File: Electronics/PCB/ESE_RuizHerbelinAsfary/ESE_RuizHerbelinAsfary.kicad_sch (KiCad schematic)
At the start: 0 parts

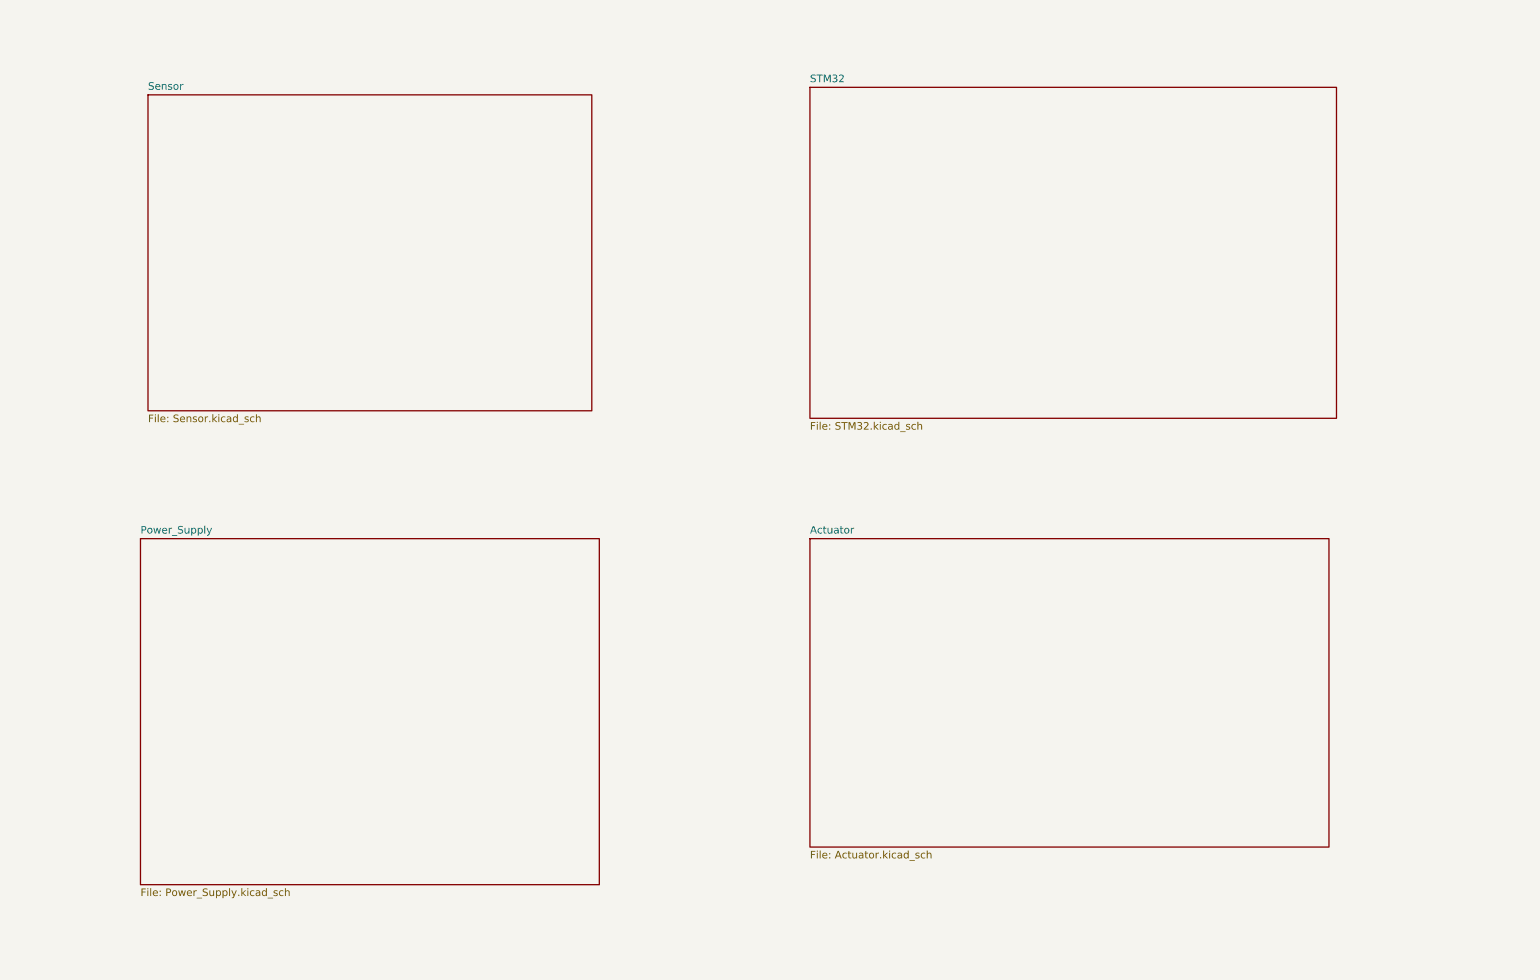
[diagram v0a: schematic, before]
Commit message: added test pin
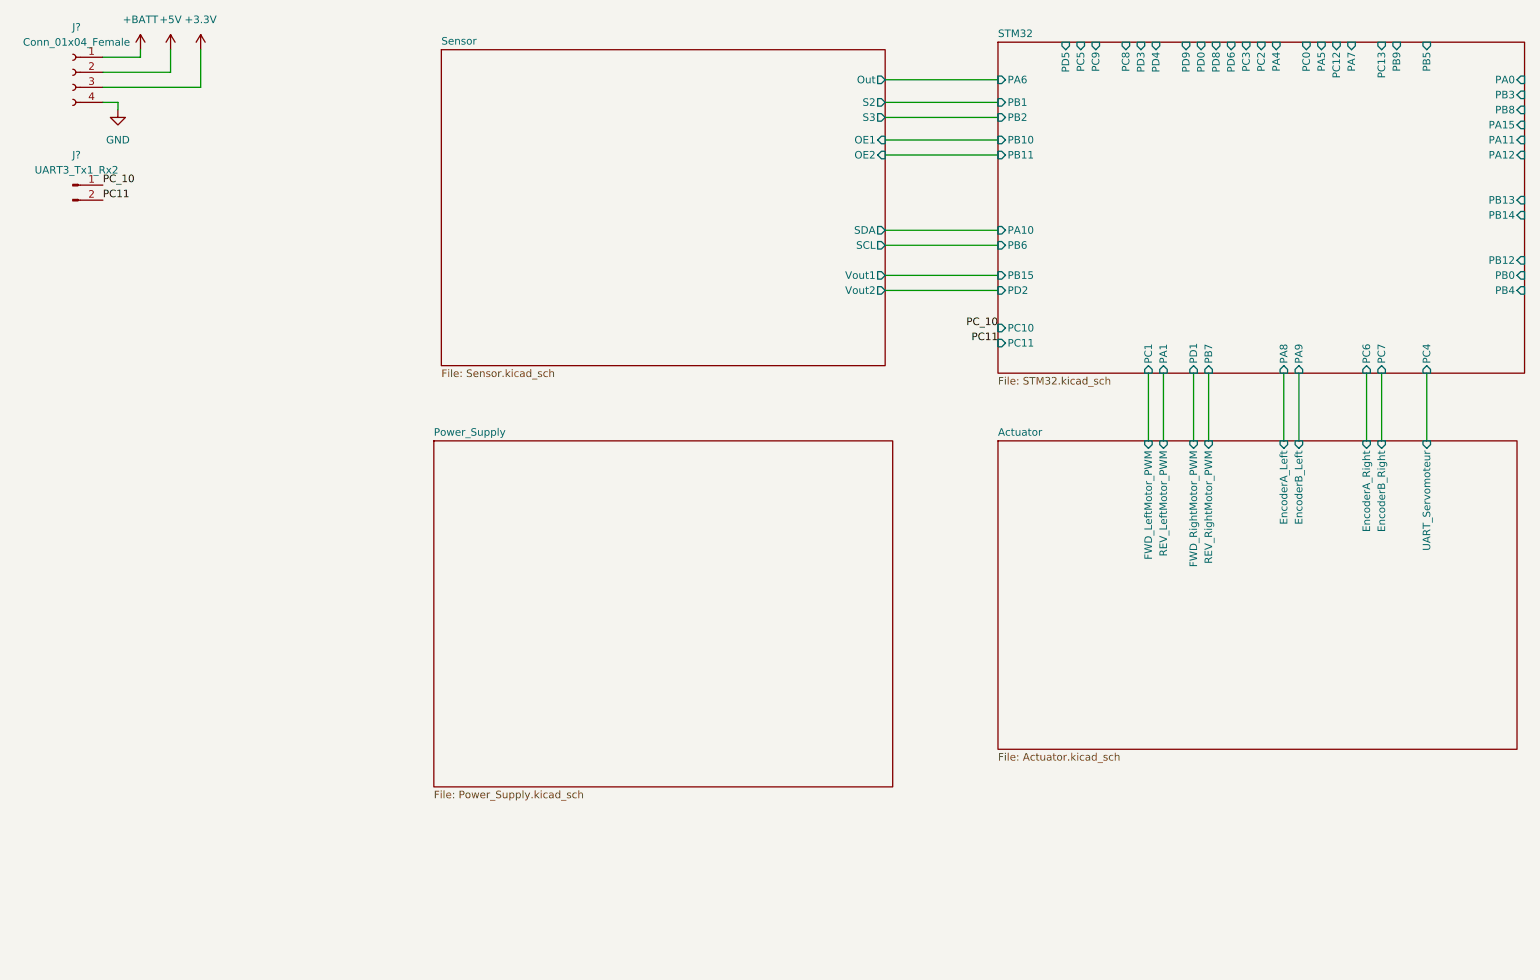
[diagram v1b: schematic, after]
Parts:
- added J?: Conn_01x04_Female, symbol Connector:Conn_01x04_Female
- added J?: UART3_Tx1_Rx2, symbol Connector:Conn_01x02_Male
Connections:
- new net +3.3V: J?.3 (Pin_3)
- new net +5V: J?.2 (Pin_2)
- new net +BATT: J?.1 (Pin_1)
- new net GND: J?.4 (Pin_4)
- new net PC11: J?.2 (Pin_2)
- new net PC_10: J?.1 (Pin_1)
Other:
- sheet Actuator ports: added EncoderA_Left, EncoderA_Right, EncoderB_Left, EncoderB_Right, FWD_LeftMotor_PWM, FWD_RightMotor_PWM, REV_LeftMotor_PWM, REV_RightMotor_PWM, UART_Servomoteur; removed none
- sheet STM32 ports: added PA0, PA1, PA10, PA11, PA12, PA15, PA4, PA5, PA6, PA7, PA8, PA9, PB0, PB1, PB10, PB11, PB12, PB13, PB14, PB15, PB2, PB3, PB4, PB5, PB6, PB7, PB8, PB9, PC0, PC1, PC10, PC11, PC12, PC13, PC2, PC3, PC4, PC5, PC6, PC7, PC8, PC9, PD0, PD1, PD2, PD3, PD4, PD5, PD6, PD8, PD9; removed none
- sheet Sensor ports: added OE1, OE2, Out, S2, S3, SCL, SDA, Vout1, Vout2; removed none

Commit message: PCB finished
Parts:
- added J101, J104: I2C1, symbol Connector:Conn_01x04_Male
- added J105: MTRX_test, symbol Connector:Conn_01x04_Female
- J102: renamed from J?; value Conn_01x04_Female -> MTRX_test
- J103: renamed from J?; value UART3_Tx1_Rx2 -> UART3
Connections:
- net +3.3V: now also J105.3 (Pin_3)
- net +5V: now also J101.2 (Pin_2), J104.2 (Pin_2), J105.2 (Pin_2)
- net +BATT: now also J105.1 (Pin_1)
- net GND: now also J101.1 (Pin_1), J104.1 (Pin_1), J105.4 (Pin_4)
- net PC11 renamed UART_Rx
- net PC_10 renamed UART_Tx
- new net SCL: J101.4 (Pin_4), J104.4 (Pin_4)
- new net SDA: J101.3 (Pin_3), J104.3 (Pin_3)
- no-connect marks 0 -> 31
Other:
- sheet STM32 ports: added PC14, PC15; removed PA0, PC3
- moved on the sheet: J102, J103

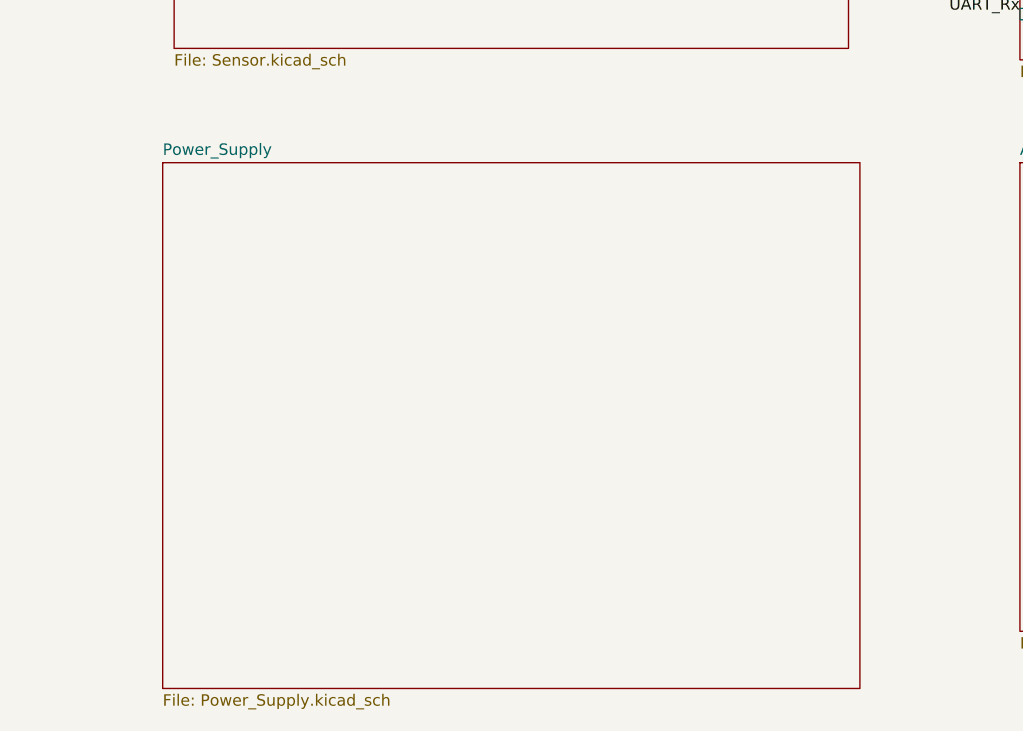
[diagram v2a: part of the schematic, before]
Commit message: added solderbridge before and after the driver
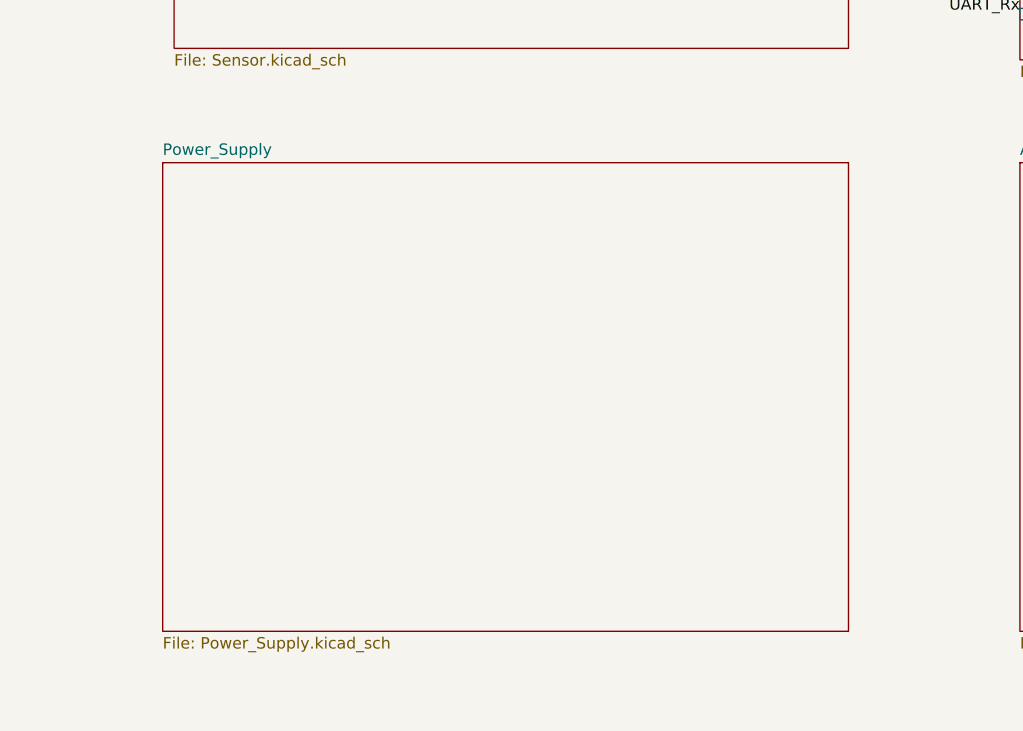
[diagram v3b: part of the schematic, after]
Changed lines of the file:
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@@
     )
   )
-  (sheet (at 82.55 91.44) (size 77.47 58.42) (fields_autoplaced)
+  (sheet (at 82.55 91.44) (size 76.2 52.07) (fields_autoplaced)
     (stroke (width 0.1524) (type solid) (color 0 0 0 0))
     (fill (color 0 0 0 0.0000))
@@
       (effects (font (size 1.27 1.27)) (justify left bottom))
     )
-    (property "Sheet file" "Power_Supply.kicad_sch" (id 1) (at 82.55 150.4446 0)
+    (property "Sheet file" "Power_Supply.kicad_sch" (id 1) (at 82.55 144.0946 0)
       (effects (font (size 1.27 1.27)) (justify left top))
     )
@@
       (reference "JP304") (unit 1) (value "SolderJumper_2_Open") (footprint "Jumper:SolderJumper-2_P1.3mm_Open_TrianglePad1.0x1.5mm")
     )
+    (path "/40bbd4bc-312d-49bd-88f6-2ab9dae3d019/5dc02104-21f7-4f53-9061-38b6726af5c5"
+      (reference "JP501") (unit 1) (value "SolderJumper_2_Open") (footprint "")
+    )
+    (path "/40bbd4bc-312d-49bd-88f6-2ab9dae3d019/54a8f4e5-28a8-4fc1-90d3-f20d46e96ad6"
+      (reference "JP502") (unit 1) (value "SolderJumper_2_Open") (footprint "")
+    )
+    (path "/40bbd4bc-312d-49bd-88f6-2ab9dae3d019/bc740fd3-668f-4267-ac36-312e4e5fa39b"
+      (reference "JP503") (unit 1) (value "SolderJumper_2_Open") (footprint "")
+    )
+    (path "/40bbd4bc-312d-49bd-88f6-2ab9dae3d019/83365208-79ca-41b0-93fa-216402934a32"
+      (reference "JP504") (unit 1) (value "SolderJumper_2_Open") (footprint "")
+    )
+    (path "/40bbd4bc-312d-49bd-88f6-2ab9dae3d019/8659013f-857b-45d1-95b7-d7905afd2a1a"
+      (reference "JP505") (unit 1) (value "SolderJumper_2_Open") (footprint "")
+    )
+    (path "/40bbd4bc-312d-49bd-88f6-2ab9dae3d019/a0cccba3-27a4-4ade-bfe9-13adaf4125e9"
+      (reference "JP506") (unit 1) (value "SolderJumper_2_Open") (footprint "")
+    )
+    (path "/40bbd4bc-312d-49bd-88f6-2ab9dae3d019/a5f7af30-ad0f-4f3a-ab85-fb2520afcaa8"
+      (reference "JP507") (unit 1) (value "SolderJumper_2_Open") (footprint "")
+    )
+    (path "/40bbd4bc-312d-49bd-88f6-2ab9dae3d019/6d9ec327-a8f1-4d49-b44f-b2ca5f46cbe0"
+      (reference "JP508") (unit 1) (value "SolderJumper_2_Open") (footprint "")
+    )
     (path "/6b2f643a-955a-47ef-920e-70e4f09a6662/29b03a20-4b8e-4936-9a55-9ac0bf668a19"

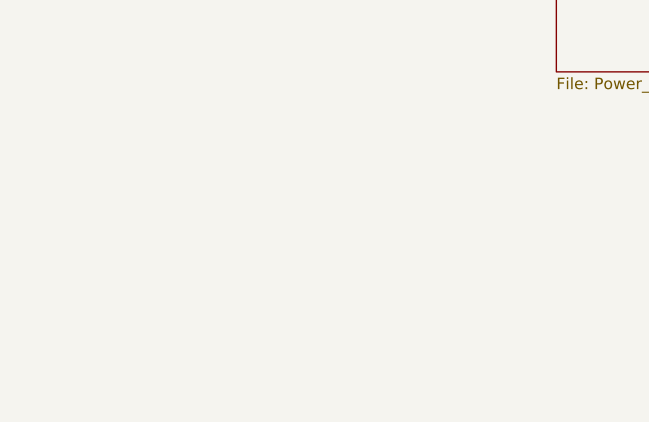
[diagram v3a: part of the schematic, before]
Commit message: added mounting hole
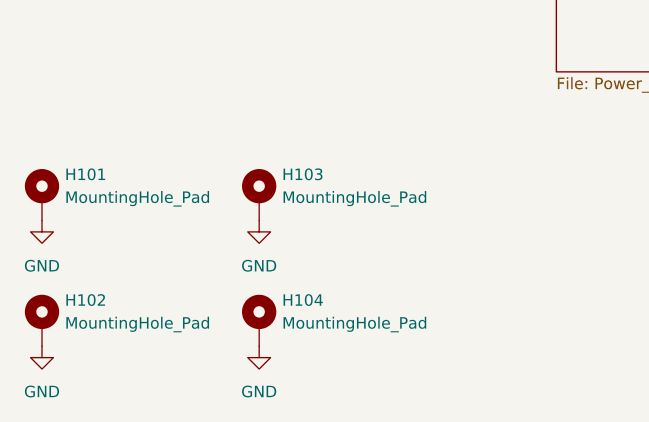
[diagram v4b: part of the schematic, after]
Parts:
- added H101, H102, H103, H104: MountingHole_Pad, symbol Mechanical:MountingHole_Pad
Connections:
- net GND: now also H101.1, H102.1, H103.1, H104.1
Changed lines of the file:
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@@
     (effects (font (size 1.27 1.27)) (justify left bottom))
+  )
+  (symbol (lib_id "power:GND") (at 49.53 160.02 0) (unit 1)
+    (in_bom yes) (on_board yes) (fields_autoplaced)
+    (property "Reference" "#PWR0115" (id 0) (at 49.53 166.37 0)
+      (effects (font (size 1.27 1.27)) hide)
+    )
+    (property "Value" "GND" (id 1) (at 49.53 165.1 0))
+    (property "Footprint" "" (id 2) (at 49.53 160.02 0)
+      (effects (font (size 1.27 1.27)) hide)
+    )
+    (property "Datasheet" "" (id 3) (at 49.53 160.02 0)
+      (effects (font (size 1.27 1.27)) hide)
+    )
+    (pin "1")
   )
   (symbol (lib_id "power:GND") (at 39.37 106.68 0) (unit 1)
@@
     )
     (property "Datasheet" "" (id 3) (at 39.37 106.68 0)
+      (effects (font (size 1.27 1.27)) hide)
+    )
+    (pin "1")
+  )
+  (symbol (lib_id "power:GND") (at 49.53 173.99 0) (unit 1)
+    (in_bom yes) (on_board yes) (fields_autoplaced)
+    (property "Reference" "#PWR0116" (id 0) (at 49.53 180.34 0)
+      (effects (font (size 1.27 1.27)) hide)
+    )
+    (property "Value" "GND" (id 1) (at 49.53 179.07 0))
+    (property "Footprint" "" (id 2) (at 49.53 173.99 0)
+      (effects (font (size 1.27 1.27)) hide)
+    )
+    (property "Datasheet" "" (id 3) (at 49.53 173.99 0)
       (effects (font (size 1.27 1.27)) hide)
     )
@@
     (pin "1")
   )
+  (symbol (lib_id "Mechanical:MountingHole_Pad") (at 49.53 157.48 0) (unit 1)
+    (in_bom yes) (on_board yes) (fields_autoplaced)
+    (property "Reference" "H103" (id 0) (at 52.07 154.9399 0)
+      (effects (font (size 1.27 1.27)) (justify left))
+    )
+    (property "Value" "MountingHole_Pad" (id 1) (at 52.07 157.4799 0)
+      (effects (font (size 1.27 1.27)) (justify left))
+    )
+    (property "Footprint" "" (id 2) (at 49.53 157.48 0)
+      (effects (font (size 1.27 1.27)) hide)
+    )
+    (property "Datasheet" "~" (id 3) (at 49.53 157.48 0)
+      (effects (font (size 1.27 1.27)) hide)
+    )
+    (pin "1")
+  )
   (symbol (lib_id "power:GND") (at 35.56 59.69 0) (unit 1)
     (in_bom yes) (on_board yes) (fields_autoplaced)
@@
     (pin "2")
   )
+  (symbol (lib_id "Mechanical:MountingHole_Pad") (at 25.4 171.45 0) (unit 1)
+    (in_bom yes) (on_board yes) (fields_autoplaced)
+    (property "Reference" "H102" (id 0) (at 27.94 168.9099 0)
+      (effects (font (size 1.27 1.27)) (justify left))
+    )
+    (property "Value" "MountingHole_Pad" (id 1) (at 27.94 171.4499 0)
+      (effects (font (size 1.27 1.27)) (justify left))
+    )
+    (property "Footprint" "" (id 2) (at 25.4 171.45 0)
+      (effects (font (size 1.27 1.27)) hide)
+    )
+    (property "Datasheet" "~" (id 3) (at 25.4 171.45 0)
+      (effects (font (size 1.27 1.27)) hide)
+    )
+    (pin "1")
+  )
   (symbol (lib_id "power:+5V") (at 44.45 25.4 0) (unit 1)
     (in_bom yes) (on_board yes) (fields_autoplaced)
@@
     (pin "1")
   )
+  (symbol (lib_id "power:GND") (at 25.4 173.99 0) (unit 1)
+    (in_bom yes) (on_board yes) (fields_autoplaced)
+    (property "Reference" "#PWR0114" (id 0) (at 25.4 180.34 0)
+      (effects (font (size 1.27 1.27)) hide)
+    )
+    (property "Value" "GND" (id 1) (at 25.4 179.07 0))
+    (property "Footprint" "" (id 2) (at 25.4 173.99 0)
+      (effects (font (size 1.27 1.27)) hide)
+    )
+    (property "Datasheet" "" (id 3) (at 25.4 173.99 0)
+      (effects (font (size 1.27 1.27)) hide)
+    )
+    (pin "1")
+  )
   (symbol (lib_id "power:+5V") (at 35.56 85.09 0) (unit 1)
     (in_bom yes) (on_board yes) (fields_autoplaced)
@@
     )
     (property "Datasheet" "" (id 3) (at 35.56 85.09 0)
+      (effects (font (size 1.27 1.27)) hide)
+    )
+    (pin "1")
+  )
+  (symbol (lib_id "Mechanical:MountingHole_Pad") (at 25.4 157.48 0) (unit 1)
+    (in_bom yes) (on_board yes) (fields_autoplaced)
+    (property "Reference" "H101" (id 0) (at 27.94 154.9399 0)
+      (effects (font (size 1.27 1.27)) (justify left))
+    )
+    (property "Value" "MountingHole_Pad" (id 1) (at 27.94 157.4799 0)
+      (effects (font (size 1.27 1.27)) (justify left))
+    )
+    (property "Footprint" "" (id 2) (at 25.4 157.48 0)
+      (effects (font (size 1.27 1.27)) hide)
+    )
+    (property "Datasheet" "~" (id 3) (at 25.4 157.48 0)
       (effects (font (size 1.27 1.27)) hide)
     )
@@
     (pin "4")
   )
+  (symbol (lib_id "Mechanical:MountingHole_Pad") (at 49.53 171.45 0) (unit 1)
+    (in_bom yes) (on_board yes) (fields_autoplaced)
+    (property "Reference" "H104" (id 0) (at 52.07 168.9099 0)
+      (effects (font (size 1.27 1.27)) (justify left))
+    )
+    (property "Value" "MountingHole_Pad" (id 1) (at 52.07 171.4499 0)
+      (effects (font (size 1.27 1.27)) (justify left))
+    )
+    (property "Footprint" "" (id 2) (at 49.53 171.45 0)
+      (effects (font (size 1.27 1.27)) hide)
+    )
+    (property "Datasheet" "~" (id 3) (at 49.53 171.45 0)
+      (effects (font (size 1.27 1.27)) hide)
+    )
+    (pin "1")
+  )
   (symbol (lib_id "Connector:Conn_01x04_Male") (at 27.94 88.9 0) (unit 1)
     (in_bom yes) (on_board yes) (fields_autoplaced)
@@
     )
     (property "Datasheet" "" (id 3) (at 49.53 25.4 0)
+      (effects (font (size 1.27 1.27)) hide)
+    )
+    (pin "1")
+  )
+  (symbol (lib_id "power:GND") (at 25.4 160.02 0) (unit 1)
+    (in_bom yes) (on_board yes) (fields_autoplaced)
+    (property "Reference" "#PWR0113" (id 0) (at 25.4 166.37 0)
+      (effects (font (size 1.27 1.27)) hide)
+    )
+    (property "Value" "GND" (id 1) (at 25.4 165.1 0))
+    (property "Footprint" "" (id 2) (at 25.4 160.02 0)
+      (effects (font (size 1.27 1.27)) hide)
+    )
+    (property "Datasheet" "" (id 3) (at 25.4 160.02 0)
       (effects (font (size 1.27 1.27)) hide)
     )
@@
       (reference "#PWR0112") (unit 1) (value "+3.3V") (footprint "")
     )
+    (path "/fdeb3dcf-a235-44b1-8a37-008fbd205346"
+      (reference "#PWR0113") (unit 1) (value "GND") (footprint "")
+    )
+    (path "/8d212c4c-30e6-473f-91fc-6f55cd805cfb"
+      (reference "#PWR0114") (unit 1) (value "GND") (footprint "")
+    )
+    (path "/13c95556-b768-47a2-8385-031c7ff1951e"
+      (reference "#PWR0115") (unit 1) (value "GND") (footprint "")
+    )
+    (path "/1e731074-dac7-4061-9e07-3ffecd647788"
+      (reference "#PWR0116") (unit 1) (value "GND") (footprint "")
+    )
     (path "/2924da36-dbac-4d9a-b64c-88077c1fc53b/69765ee5-1e73-4839-8b77-5916e7a4ad61"
       (reference "#PWR0201") (unit 1) (value "~") (footprint "")
@@
       (reference "D303") (unit 1) (value "Red") (footprint "LED_SMD:LED_0603_1608Metric_Pad1.05x0.95mm_HandSolder")
     )
+    (path "/a699aea8-c41e-4e46-bb31-256a11b00f2e"
+      (reference "H101") (unit 1) (value "MountingHole_Pad") (footprint "")
+    )
+    (path "/7082ada9-a783-424b-ade2-b453fc714d2d"
+      (reference "H102") (unit 1) (value "MountingHole_Pad") (footprint "")
+    )
+    (path "/5580a26b-8e53-4e07-b5ba-06476c6fad37"
+      (reference "H103") (unit 1) (value "MountingHole_Pad") (footprint "")
+    )
+    (path "/d033cf4c-5de0-4641-b026-02388b00c3f6"
+      (reference "H104") (unit 1) (value "MountingHole_Pad") (footprint "")
+    )
     (path "/d631131a-f60a-4505-aee8-badeed1e432b"
